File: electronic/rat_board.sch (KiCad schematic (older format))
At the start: 49 parts, among them P1 FRONT_LEFT_IR, P2 SIDE_LEFT_IR, P3 SIDE_RIGHT_IR, P4 FRONT_RIGHT_IR, P5 LEFT_MOTOR, P6 RIGHT_MOTOR, P7 JTAG, P8 CONN_01X02, SW1 SW_PUSH_SMALL_H, SW2 SWITCH_INV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

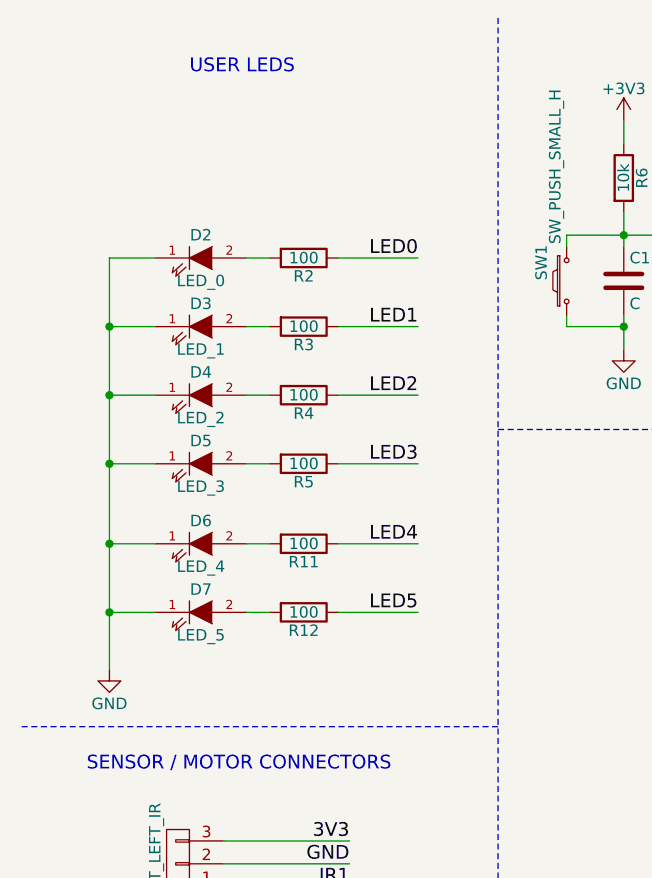
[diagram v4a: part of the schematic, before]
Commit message: logos and filled zones
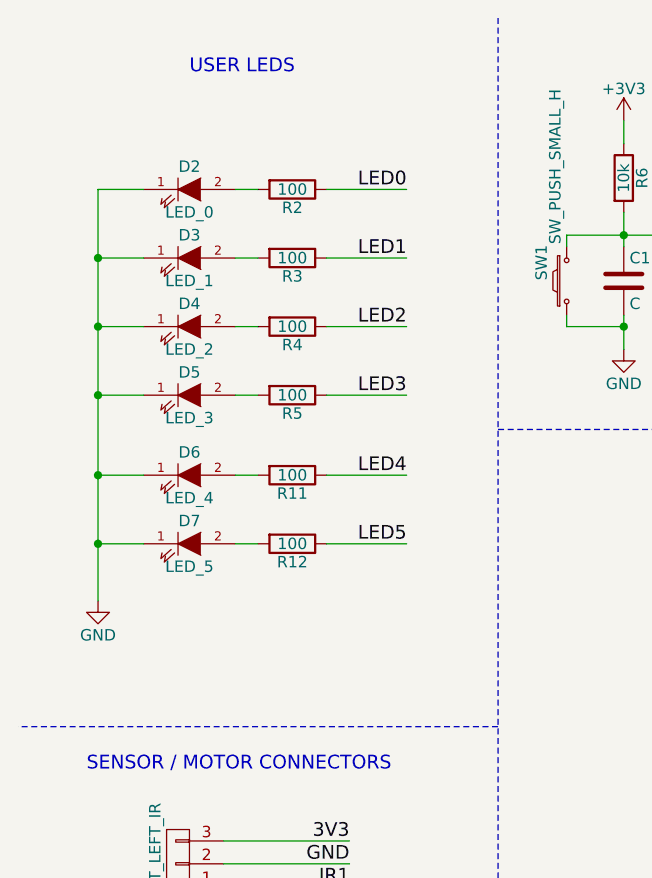
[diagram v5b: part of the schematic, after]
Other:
- moved on the sheet: D2, D3, D4, D5, D6, D7, R11, R12, R2, R3, R4, R5
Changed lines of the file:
@@
 L LED D2
 U 1 1 58795064
-P 1300 1550
-F 0 "D2" H 1300 1650 50  0000 C CNN
-F 1 "LED_0" H 1300 1450 50  0000 C CNN
-F 2 "LEDs:LED-3MM" H 1300 1550 50  0001 C CNN
-F 3 "" H 1300 1550 50  0000 C CNN
-	1    1300 1550
+P 1250 1250
+F 0 "D2" H 1250 1350 50  0000 C CNN
+F 1 "LED_0" H 1250 1150 50  0000 C CNN
+F 2 "LEDs:LED-3MM" H 1250 1250 50  0001 C CNN
+F 3 "" H 1250 1250 50  0000 C CNN
+	1    1250 1250
 	1    0    0    -1
 $EndComp
@@
 L R R2
 U 1 1 5879506A
-P 1750 1550
-F 0 "R2" V 1830 1550 50  0000 C CNN
-F 1 "100" V 1750 1550 50  0000 C CNN
-F 2 "Resistors_SMD:R_0603_HandSoldering" V 1680 1550 50  0001 C CNN
-F 3 "" H 1750 1550 50  0000 C CNN
-	1    1750 1550
+P 1700 1250
+F 0 "R2" V 1780 1250 50  0000 C CNN
+F 1 "100" V 1700 1250 50  0000 C CNN
+F 2 "Resistors_SMD:R_0603_HandSoldering" V 1630 1250 50  0001 C CNN
+F 3 "" H 1700 1250 50  0000 C CNN
+	1    1700 1250
 	0    1    1    0
 $EndComp
@@
 L LED D3
 U 1 1 587952A8
-P 1300 1850
-F 0 "D3" H 1300 1950 50  0000 C CNN
-F 1 "LED_1" H 1300 1750 50  0000 C CNN
-F 2 "LEDs:LED-3MM" H 1300 1850 50  0001 C CNN
-F 3 "" H 1300 1850 50  0000 C CNN
-	1    1300 1850
+P 1250 1550
+F 0 "D3" H 1250 1650 50  0000 C CNN
+F 1 "LED_1" H 1250 1450 50  0000 C CNN
+F 2 "LEDs:LED-3MM" H 1250 1550 50  0001 C CNN
+F 3 "" H 1250 1550 50  0000 C CNN
+	1    1250 1550
 	1    0    0    -1
 $EndComp
@@
 L LED D4
 U 1 1 58795367
-P 1300 2150
-F 0 "D4" H 1300 2250 50  0000 C CNN
-F 1 "LED_2" H 1300 2050 50  0000 C CNN
-F 2 "LEDs:LED-3MM" H 1300 2150 50  0001 C CNN
-F 3 "" H 1300 2150 50  0000 C CNN
-	1    1300 2150
+P 1250 1850
+F 0 "D4" H 1250 1950 50  0000 C CNN
+F 1 "LED_2" H 1250 1750 50  0000 C CNN
+F 2 "LEDs:LED-3MM" H 1250 1850 50  0001 C CNN
+F 3 "" H 1250 1850 50  0000 C CNN
+	1    1250 1850
 	1    0    0    -1
 $EndComp
@@
 L LED D5
 U 1 1 587954A6
-P 1300 2450
-F 0 "D5" H 1300 2550 50  0000 C CNN
-F 1 "LED_3" H 1300 2350 50  0000 C CNN
-F 2 "LEDs:LED-3MM" H 1300 2450 50  0001 C CNN
-F 3 "" H 1300 2450 50  0000 C CNN
-	1    1300 2450
+P 1250 2150
+F 0 "D5" H 1250 2250 50  0000 C CNN
+F 1 "LED_3" H 1250 2050 50  0000 C CNN
+F 2 "LEDs:LED-3MM" H 1250 2150 50  0001 C CNN
+F 3 "" H 1250 2150 50  0000 C CNN
+	1    1250 2150
 	1    0    0    -1
 $EndComp
@@
 L GND #PWR020
 U 1 1 5879584C
-P 900 3350
-F 0 "#PWR020" H 900 3100 50  0001 C CNN
-F 1 "GND" H 900 3200 50  0000 C CNN
-F 2 "" H 900 3350 50  0000 C CNN
-F 3 "" H 900 3350 50  0000 C CNN
-	1    900  3350
-	1    0    0    -1
-$EndComp
-Text Label 2250 1850 2    60   ~ 0
+P 850 3050
+F 0 "#PWR020" H 850 2800 50  0001 C CNN
+F 1 "GND" H 850 2900 50  0000 C CNN
+F 2 "" H 850 3050 50  0000 C CNN
+F 3 "" H 850 3050 50  0000 C CNN
+	1    850  3050
+	1    0    0    -1
+$EndComp
+Text Label 2200 1550 2    60   ~ 0
 LED1
-Text Label 2250 2150 2    60   ~ 0
+Text Label 2200 1850 2    60   ~ 0
 LED2
-Text Label 2250 2450 2    60   ~ 0
+Text Label 2200 2150 2    60   ~ 0
 LED3
 $Comp
@@
 L R R3
 U 1 1 587A2320
-P 1750 1850
-F 0 "R3" V 1830 1850 50  0000 C CNN
-F 1 "100" V 1750 1850 50  0000 C CNN
-F 2 "Resistors_SMD:R_0603_HandSoldering" V 1680 1850 50  0001 C CNN
-F 3 "" H 1750 1850 50  0000 C CNN
-	1    1750 1850
+P 1700 1550
+F 0 "R3" V 1780 1550 50  0000 C CNN
+F 1 "100" V 1700 1550 50  0000 C CNN
+F 2 "Resistors_SMD:R_0603_HandSoldering" V 1630 1550 50  0001 C CNN
+F 3 "" H 1700 1550 50  0000 C CNN
+	1    1700 1550
 	0    1    1    0
 $EndComp
@@
 L R R4
 U 1 1 587A23EC
-P 1750 2150
-F 0 "R4" V 1830 2150 50  0000 C CNN
-F 1 "100" V 1750 2150 50  0000 C CNN
-F 2 "Resistors_SMD:R_0603_HandSoldering" V 1680 2150 50  0001 C CNN
-F 3 "" H 1750 2150 50  0000 C CNN
-	1    1750 2150
+P 1700 1850
+F 0 "R4" V 1780 1850 50  0000 C CNN
+F 1 "100" V 1700 1850 50  0000 C CNN
+F 2 "Resistors_SMD:R_0603_HandSoldering" V 1630 1850 50  0001 C CNN
+F 3 "" H 1700 1850 50  0000 C CNN
+	1    1700 1850
 	0    1    1    0
 $EndComp
@@
 L R R5
 U 1 1 587A24B8
-P 1750 2450
-F 0 "R5" V 1830 2450 50  0000 C CNN
-F 1 "100" V 1750 2450 50  0000 C CNN
-F 2 "Resistors_SMD:R_0603_HandSoldering" V 1680 2450 50  0001 C CNN
-F 3 "" H 1750 2450 50  0000 C CNN
-	1    1750 2450
+P 1700 2150
+F 0 "R5" V 1780 2150 50  0000 C CNN
+F 1 "100" V 1700 2150 50  0000 C CNN
+F 2 "Resistors_SMD:R_0603_HandSoldering" V 1630 2150 50  0001 C CNN
+F 3 "" H 1700 2150 50  0000 C CNN
+	1    1700 2150
 	0    1    1    0
 $EndComp
@@
 	10700 1050 10700 1500
 Wire Wire Line
-	900  1550 1100 1550
-Wire Wire Line
-	1500 1550 1600 1550
-Wire Wire Line
-	1900 1850 2250 1850
-Wire Wire Line
-	900  1850 1100 1850
-Wire Wire Line
-	1500 1850 1600 1850
-Wire Wire Line
-	1900 2150 2250 2150
-Wire Wire Line
-	900  2150 1100 2150
-Wire Wire Line
-	1500 2150 1600 2150
-Wire Wire Line
-	1900 2450 2250 2450
-Wire Wire Line
-	900  2450 1100 2450
-Wire Wire Line
-	1500 2450 1600 2450
-Connection ~ 900  1850
-Connection ~ 900  2150
-Connection ~ 900  2450
+	850  1250 1050 1250
+Wire Wire Line
+	1450 1250 1550 1250
+Wire Wire Line
+	1850 1550 2200 1550
+Wire Wire Line
+	850  1550 1050 1550
+Wire Wire Line
+	1450 1550 1550 1550
+Wire Wire Line
+	1850 1850 2200 1850
+Wire Wire Line
+	850  1850 1050 1850
+Wire Wire Line
+	1450 1850 1550 1850
+Wire Wire Line
+	1850 2150 2200 2150
+Wire Wire Line
+	850  2150 1050 2150
+Wire Wire Line
+	1450 2150 1550 2150
+Connection ~ 850  1550
+Connection ~ 850  1850
+Connection ~ 850  2150
 Connection ~ 3150 1850
 Wire Wire Line
@@
 Wire Wire Line
 	7650 1000 7650 1400
-Text Label 2250 1550 2    60   ~ 0
+Text Label 2200 1250 2    60   ~ 0
 LED0
 Wire Wire Line
-	1900 1550 2250 1550
-Wire Wire Line
-	900  1550 900  3350
+	1850 1250 2200 1250
+Wire Wire Line
+	850  1250 850  3050
 $Comp
 L LED D6
 U 1 1 5886AB08
-P 1300 2800
-F 0 "D6" H 1300 2900 50  0000 C CNN
-F 1 "LED_4" H 1300 2700 50  0000 C CNN
-F 2 "LEDs:LED-3MM" H 1300 2800 50  0001 C CNN
-F 3 "" H 1300 2800 50  0000 C CNN
-	1    1300 2800
+P 1250 2500
+F 0 "D6" H 1250 2600 50  0000 C CNN
+F 1 "LED_4" H 1250 2400 50  0000 C CNN
+F 2 "LEDs:LED-3MM" H 1250 2500 50  0001 C CNN
+F 3 "" H 1250 2500 50  0000 C CNN
+	1    1250 2500
 	1    0    0    -1
 $EndComp
@@
 L LED D7
 U 1 1 5886AB0E
-P 1300 3100
-F 0 "D7" H 1300 3200 50  0000 C CNN
-F 1 "LED_5" H 1300 3000 50  0000 C CNN
-F 2 "LEDs:LED-3MM" H 1300 3100 50  0001 C CNN
-F 3 "" H 1300 3100 50  0000 C CNN
-	1    1300 3100
-	1    0    0    -1
-$EndComp
-Text Label 2250 2800 2    60   ~ 0
+P 1250 2800
+F 0 "D7" H 1250 2900 50  0000 C CNN
+F 1 "LED_5" H 1250 2700 50  0000 C CNN
+F 2 "LEDs:LED-3MM" H 1250 2800 50  0001 C CNN
+F 3 "" H 1250 2800 50  0000 C CNN
+	1    1250 2800
+	1    0    0    -1
+$EndComp
+Text Label 2200 2500 2    60   ~ 0
 LED4
-Text Label 2250 3100 2    60   ~ 0
+Text Label 2200 2800 2    60   ~ 0
 LED5
 $Comp
 L R R11
 U 1 1 5886AB16
-P 1750 2800
-F 0 "R11" V 1830 2800 50  0000 C CNN
-F 1 "100" V 1750 2800 50  0000 C CNN
-F 2 "Resistors_SMD:R_0603_HandSoldering" V 1680 2800 50  0001 C CNN
-F 3 "" H 1750 2800 50  0000 C CNN
-	1    1750 2800
+P 1700 2500
+F 0 "R11" V 1780 2500 50  0000 C CNN
+F 1 "100" V 1700 2500 50  0000 C CNN
+F 2 "Resistors_SMD:R_0603_HandSoldering" V 1630 2500 50  0001 C CNN
+F 3 "" H 1700 2500 50  0000 C CNN
+	1    1700 2500
 	0    1    1    0
 $EndComp
@@
 L R R12
 U 1 1 5886AB1C
-P 1750 3100
-F 0 "R12" V 1830 3100 50  0000 C CNN
-F 1 "100" V 1750 3100 50  0000 C CNN
-F 2 "Resistors_SMD:R_0603_HandSoldering" V 1680 3100 50  0001 C CNN
-F 3 "" H 1750 3100 50  0000 C CNN
-	1    1750 3100
+P 1700 2800
+F 0 "R12" V 1780 2800 50  0000 C CNN
+F 1 "100" V 1700 2800 50  0000 C CNN
+F 2 "Resistors_SMD:R_0603_HandSoldering" V 1630 2800 50  0001 C CNN
+F 3 "" H 1700 2800 50  0000 C CNN
+	1    1700 2800
 	0    1    1    0
 $EndComp
 Wire Wire Line
-	1900 2800 2250 2800
-Wire Wire Line
-	900  2800 1100 2800
-Wire Wire Line
-	1500 2800 1600 2800
-Wire Wire Line
-	1900 3100 2250 3100
-Wire Wire Line
-	900  3100 1100 3100
-Wire Wire Line
-	1500 3100 1600 3100
-Connection ~ 900  2800
-Connection ~ 900  3100
+	1850 2500 2200 2500
+Wire Wire Line
+	850  2500 1050 2500
+Wire Wire Line
+	1450 2500 1550 2500
+Wire Wire Line
+	1850 2800 2200 2800
+Wire Wire Line
+	850  2800 1050 2800
+Wire Wire Line
+	1450 2800 1550 2800
+Connection ~ 850  2500
+Connection ~ 850  2800
 Text Label 6950 1000 3    60   ~ 0
 M_PWMB

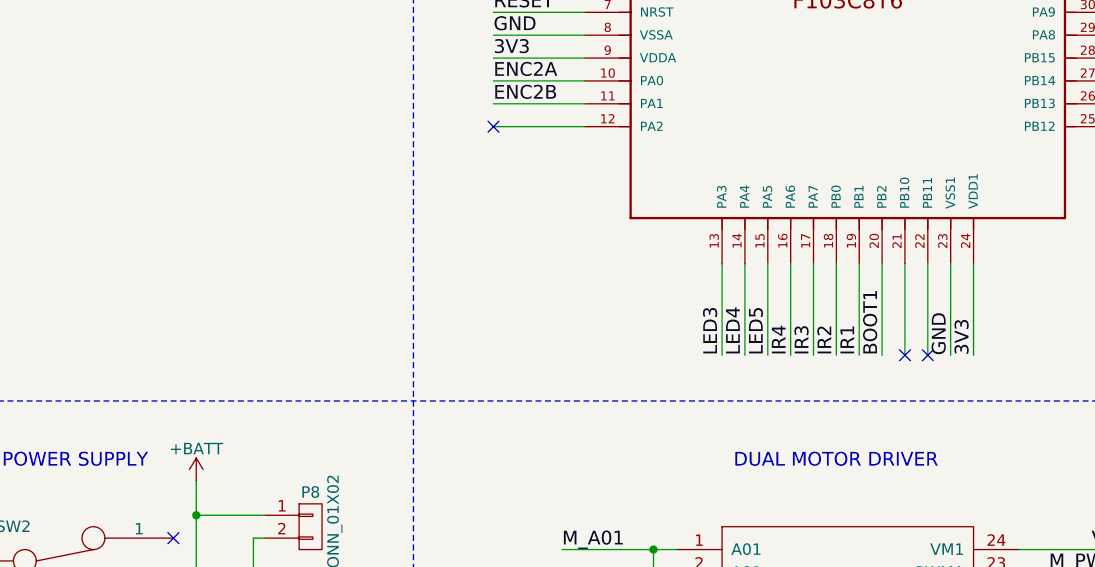
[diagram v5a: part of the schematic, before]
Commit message: added an additional uart connector
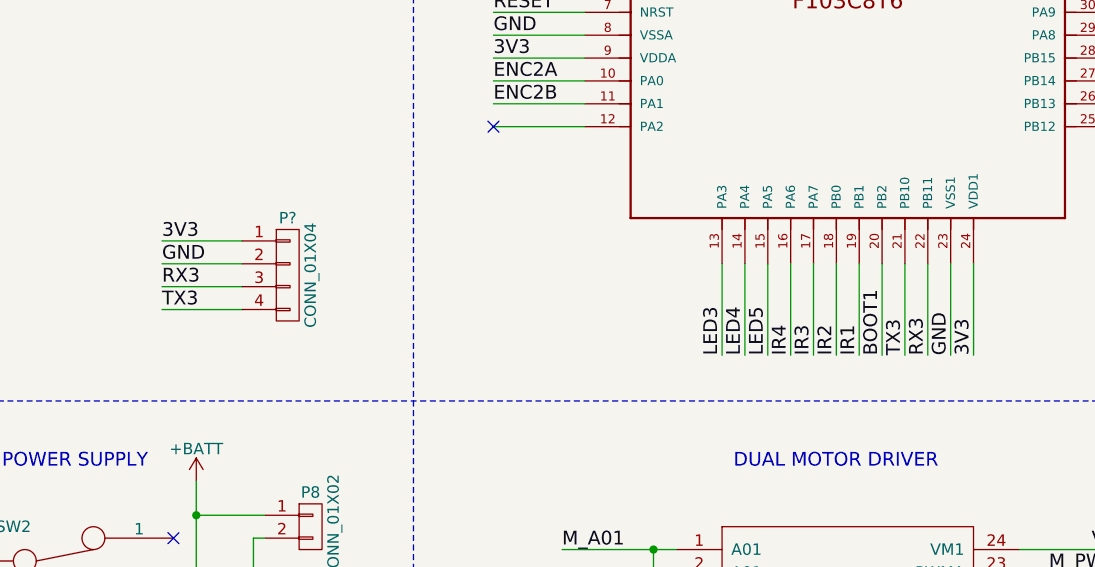
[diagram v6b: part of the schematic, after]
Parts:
- added P?: CONN_01X04, symbol CONN_01X04
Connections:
- net +3V3: now also P?.1 (P1)
- net GND: now also P?.2 (P2)
- net TX3: now reaches U3.21 (PB10)
- net TX3: now also P?.4 (P4)
- net RX3: now reaches U3.22 (PB11)
- net RX3: now also P?.3 (P3)
- no-connect marks 8 -> 6
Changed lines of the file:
@@
 NoConn ~ 8750 3100
 NoConn ~ 5650 3100
-NoConn ~ 7450 4100
-NoConn ~ 7550 4100
+$Comp
+L CONN_01X04 P?
+U 1 1 58938DC7
+P 4750 3750
+F 0 "P?" H 4750 4000 50  0000 C CNN
+F 1 "CONN_01X04" V 4850 3750 50  0000 C CNN
+F 2 "" H 4750 3750 50  0000 C CNN
+F 3 "" H 4750 3750 50  0000 C CNN
+	1    4750 3750
+	1    0    0    -1
+$EndComp
+Text Label 4200 3600 0    60   ~ 0
+3V3
+Text Label 4200 3700 0    60   ~ 0
+GND
+Text Label 7450 4100 1    60   ~ 0
+TX3
+Text Label 7550 4100 1    60   ~ 0
+RX3
+Text Label 4200 3800 0    60   ~ 0
+RX3
+Text Label 4200 3900 0    60   ~ 0
+TX3
+Wire Wire Line
+	4200 3600 4550 3600
+Wire Wire Line
+	4200 3700 4550 3700
+Wire Wire Line
+	4200 3800 4550 3800
+Wire Wire Line
+	4200 3900 4550 3900
 $EndSCHEMATC

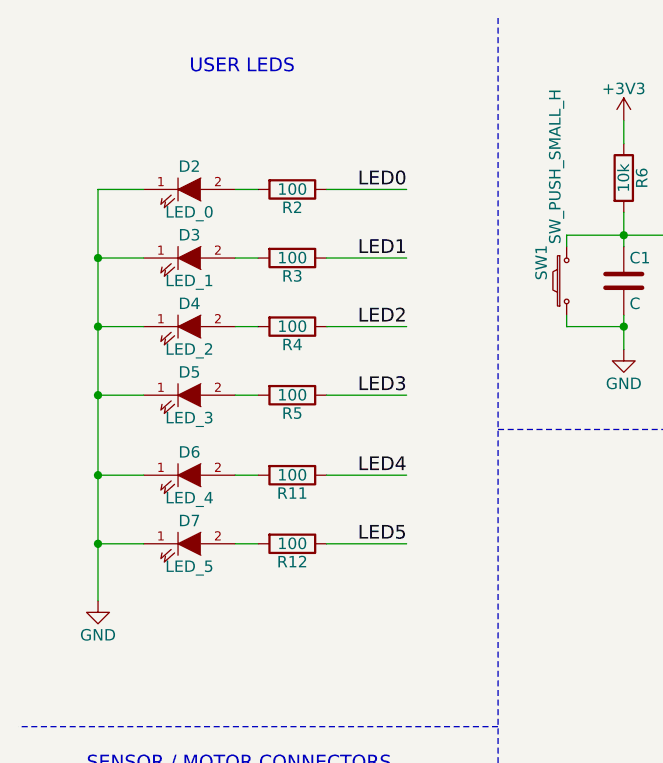
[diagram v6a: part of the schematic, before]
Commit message: smaller pushbutton on pcb
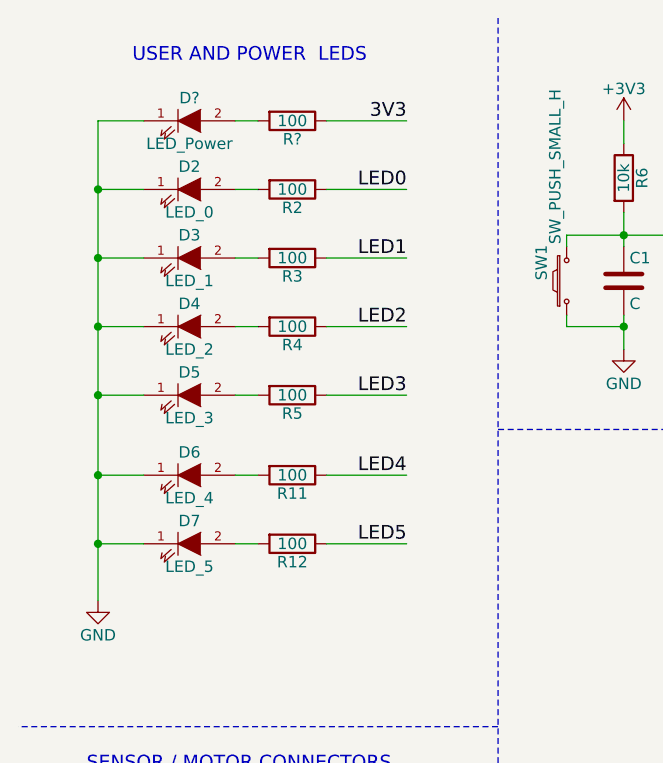
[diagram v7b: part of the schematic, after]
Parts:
- added D?: LED_Power, LEDs:LED-3MM, symbol LED
- added R?: 100, Resistors_SMD:R_0603_HandSoldering, symbol R
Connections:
- net +3V3: now also R?.1
- net GND: now also D?.1 (K)
- new net: D?.2 (A), R?.2
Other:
- note added: "USER AND POWER LEDS"
- note removed: "USER LEDS"
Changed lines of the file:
@@
 Text Notes 6600 750  0    60   ~ 0
 STM32 MICROCONTROLLER
-Text Notes 1250 750  0    60   ~ 0
-USER LEDS
+Text Notes 1000 700  0    60   ~ 0
+USER AND POWER  LEDS
 Text Notes 800  3800 0    60   ~ 0
 SENSOR / MOTOR CONNECTORS
@@
 Wire Wire Line
 	1850 1250 2200 1250
-Wire Wire Line
-	850  1250 850  3050
 $Comp
 L LED D6
@@
 Wire Wire Line
 	4200 3900 4550 3900
+$Comp
+L LED D?
+U 1 1 589F2FBF
+P 1250 950
+F 0 "D?" H 1250 1050 50  0000 C CNN
+F 1 "LED_Power" H 1250 850 50  0000 C CNN
+F 2 "LEDs:LED-3MM" H 1250 950 50  0001 C CNN
+F 3 "" H 1250 950 50  0000 C CNN
+	1    1250 950
+	1    0    0    -1
+$EndComp
+$Comp
+L R R?
+U 1 1 589F2FC5
+P 1700 950
+F 0 "R?" V 1780 950 50  0000 C CNN
+F 1 "100" V 1700 950 50  0000 C CNN
+F 2 "Resistors_SMD:R_0603_HandSoldering" V 1630 950 50  0001 C CNN
+F 3 "" H 1700 950 50  0000 C CNN
+	1    1700 950
+	0    1    1    0
+$EndComp
+Wire Wire Line
+	850  950  1050 950
+Wire Wire Line
+	1450 950  1550 950
+Wire Wire Line
+	1850 950  2200 950
+Connection ~ 850  1250
+Text Label 2200 950  2    60   ~ 0
+3V3
+Wire Wire Line
+	850  950  850  3050
 $EndSCHEMATC
